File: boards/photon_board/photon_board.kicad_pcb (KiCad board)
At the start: 2 copper layers, 2 parts, among them J1 TERASIC, J2 PHOTON

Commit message: finalize schematic
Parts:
- added C1: 1u, Capacitor_SMD:C_0603_1608Metric_Pad1.05x0.95mm_HandSolder, F.Cu at (151.5, 79.5)
- added C2: 0.1u, Capacitor_SMD:C_0603_1608Metric_Pad1.05x0.95mm_HandSolder, F.Cu at (151.5, 81.0)
- added C3: 1u, Capacitor_SMD:C_0603_1608Metric_Pad1.05x0.95mm_HandSolder, F.Cu at (154.9, 79.5)
- added C4: 0.1u, Capacitor_SMD:C_0603_1608Metric_Pad1.05x0.95mm_HandSolder, F.Cu at (154.9, 81.0)
- added U1: SN65LVDT34D, Package_SO:SOIC-8_3.9x4.9mm_P1.27mm, F.Cu at (163.8, 71.3)
- added U2: SN65LVDT34D, Package_SO:SOIC-8_3.9x4.9mm_P1.27mm, F.Cu at (163.7, 80.6)
- J1: moved to B.Cu
- moved J2 13.5 mm to (175.8, 79.4)
- turned J1 to 180 degrees
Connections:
- J1 pad 18: Net-(J1-Pad18) -> /DATA_CLK
- J1 pad 20: Net-(J1-Pad20) -> /DATA2_OUT
- J1 pad 22: Net-(J1-Pad22) -> /DATA1_OUT
- J1 pad 24: Net-(J1-Pad24) -> /DATA_SYNC
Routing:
- net /DATA2_OUT-: track 5.44 -> 0.00 mm
- net /DATA_CLK+: track 5.30 -> 0.00 mm
- net /DATA_CLK-: track 5.15 -> 0.00 mm
- net /DATA2_OUT+: track 3.95 -> 0.00 mm

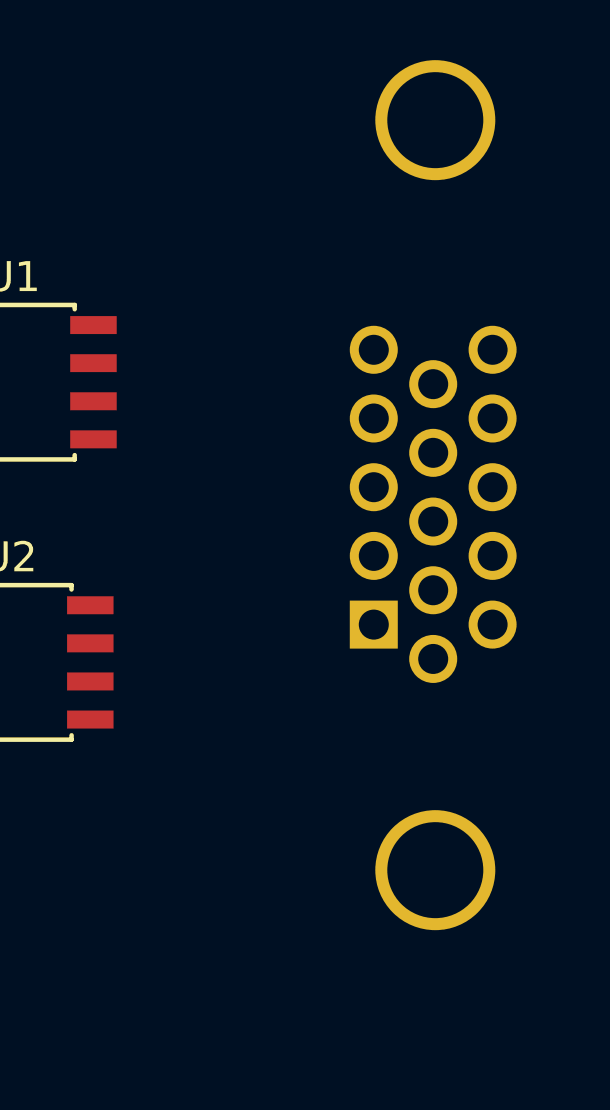
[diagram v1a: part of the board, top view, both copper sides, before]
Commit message: add connector for photon and make appropriate footprint
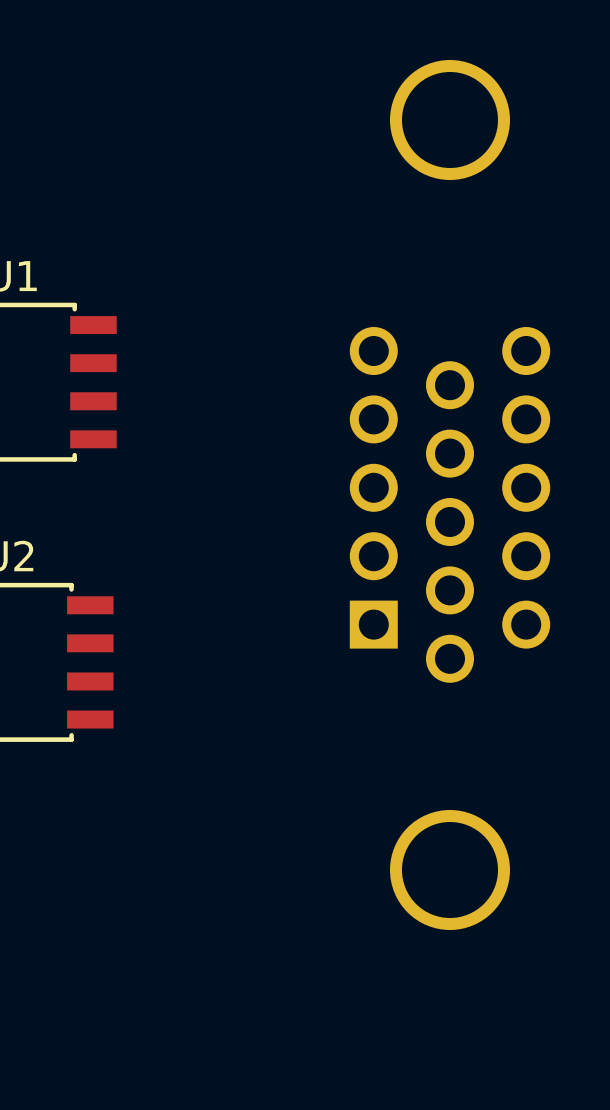
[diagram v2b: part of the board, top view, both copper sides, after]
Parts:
- J2: footprint Connector_Dsub:DSUB-15-HD_Female_Horizontal_P2.29x1.98mm_EdgePinOffset3.03mm_Housed_MountingHolesOffset4.94mm -> d_connector:DSUB-15-HD_Female_Horizontal_Pitch2.28x2.54mm_EdgePinOffset8.89mm_Housed_MountingHolesOffset11.43mm

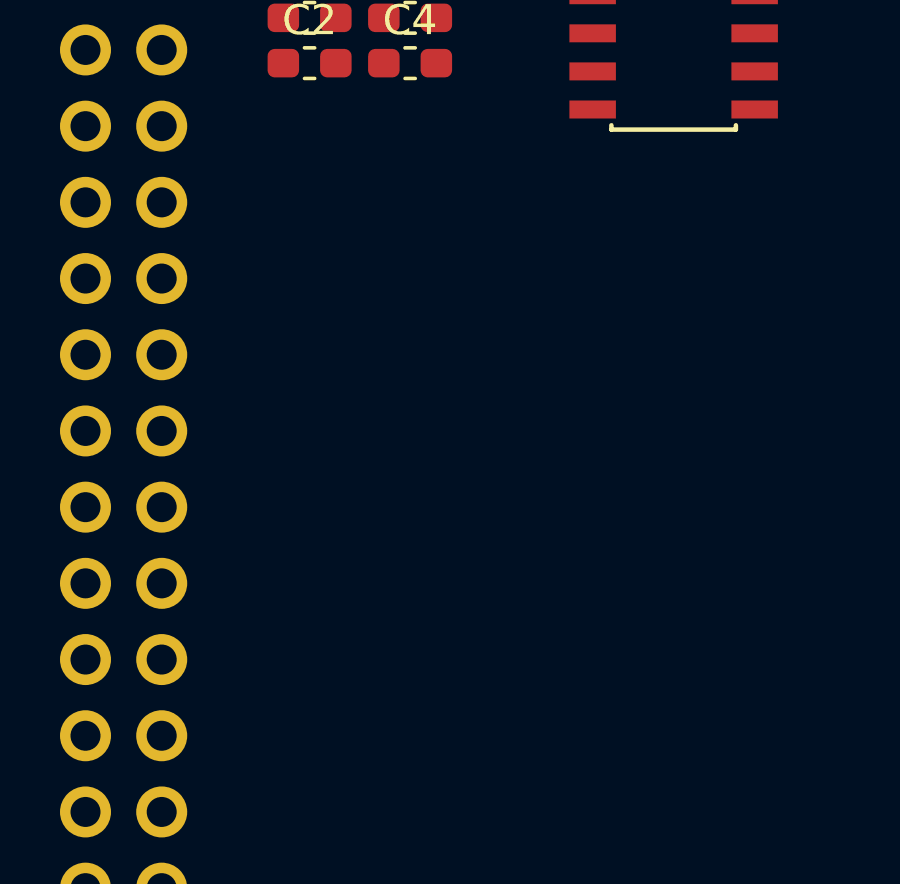
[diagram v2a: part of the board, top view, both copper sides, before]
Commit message: add data out connector for eg logic analysis
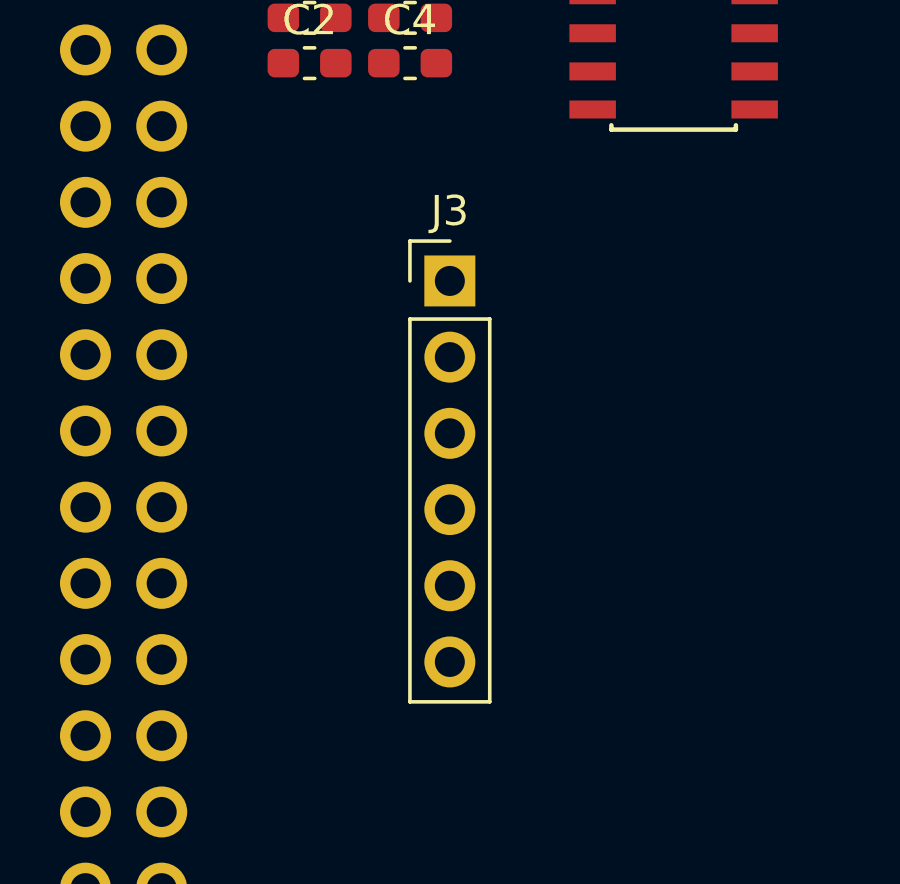
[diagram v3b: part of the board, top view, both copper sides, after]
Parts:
- added J3: DATA, Connector_PinHeader_2.54mm:PinHeader_1x06_P2.54mm_Vertical, F.Cu at (156.2, 88.3)
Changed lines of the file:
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@@
     (tracks 0)
     (zones 0)
-    (modules 8)
+    (modules 9)
     (nets 54)
   )
@@
     )
   )
+  (module Connector_PinHeader_2.54mm:PinHeader_1x06_P2.54mm_Vertical (layer F.Cu)
+    (at 156.21 88.265)
+    (descr "Through hole straight pin header, 1x06, 2.54mm pitch, single row")
+    (tags "Through hole pin header THT 1x06 2.54mm single row")
+    (fp_text reference J3 (at 0 -2.33) (layer F.SilkS)
+      (effects (font (size 1 1) (thickness 0.15)))
+    )
+    (fp_text value DATA (at 0 15.03) (layer F.Fab)
+      (effects (font (size 1 1) (thickness 0.15)))
+    )
+    (fp_line (start -0.635 -1.27) (end 1.27 -1.27) (layer F.Fab) (width 0.1))
+    (fp_line (start 1.27 -1.27) (end 1.27 13.97) (layer F.Fab) (width 0.1))
+    (fp_line (start 1.27 13.97) (end -1.27 13.97) (layer F.Fab) (width 0.1))
+    (fp_line (start -1.27 13.97) (end -1.27 -0.635) (layer F.Fab) (width 0.1))
+    (fp_line (start -1.27 -0.635) (end -0.635 -1.27) (layer F.Fab) (width 0.1))
+    (fp_line (start -1.33 14.03) (end 1.33 14.03) (layer F.SilkS) (width 0.12))
+    (fp_line (start -1.33 1.27) (end -1.33 14.03) (layer F.SilkS) (width 0.12))
+    (fp_line (start 1.33 1.27) (end 1.33 14.03) (layer F.SilkS) (width 0.12))
+    (fp_line (start -1.33 1.27) (end 1.33 1.27) (layer F.SilkS) (width 0.12))
+    (fp_line (start -1.33 0) (end -1.33 -1.33) (layer F.SilkS) (width 0.12))
+    (fp_line (start -1.33 -1.33) (end 0 -1.33) (layer F.SilkS) (width 0.12))
+    (fp_line (start -1.8 -1.8) (end -1.8 14.5) (layer F.CrtYd) (width 0.05))
+    (fp_line (start -1.8 14.5) (end 1.8 14.5) (layer F.CrtYd) (width 0.05))
+    (fp_line (start 1.8 14.5) (end 1.8 -1.8) (layer F.CrtYd) (width 0.05))
+    (fp_line (start 1.8 -1.8) (end -1.8 -1.8) (layer F.CrtYd) (width 0.05))
+    (fp_text user %R (at 0 6.35 90) (layer F.Fab)
+      (effects (font (size 1 1) (thickness 0.15)))
+    )
+    (pad 1 thru_hole rect (at 0 0) (size 1.7 1.7) (drill 1) (layers *.Cu *.Mask)
+      (net 12 GND))
+    (pad 2 thru_hole oval (at 0 2.54) (size 1.7 1.7) (drill 1) (layers *.Cu *.Mask)
+      (net 50 /DATA_CLK))
+    (pad 3 thru_hole oval (at 0 5.08) (size 1.7 1.7) (drill 1) (layers *.Cu *.Mask)
+      (net 51 /DATA2_OUT))
+    (pad 4 thru_hole oval (at 0 7.62) (size 1.7 1.7) (drill 1) (layers *.Cu *.Mask)
+      (net 52 /DATA1_OUT))
+    (pad 5 thru_hole oval (at 0 10.16) (size 1.7 1.7) (drill 1) (layers *.Cu *.Mask)
+      (net 53 /DATA_SYNC))
+    (pad 6 thru_hole oval (at 0 12.7) (size 1.7 1.7) (drill 1) (layers *.Cu *.Mask)
+      (net 12 GND))
+    (model ${KISYS3DMOD}/Connector_PinHeader_2.54mm.3dshapes/PinHeader_1x06_P2.54mm_Vertical.wrl
+      (at (xyz 0 0 0))
+      (scale (xyz 1 1 1))
+      (rotate (xyz 0 0 0))
+    )
+  )

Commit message: route board
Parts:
- moved U2 15.3 mm to (161.0, 95.8)
- moved J2 15.1 mm to (171.5, 93.8)
- moved U1 14.6 mm to (161.0, 85.6)
- moved C4 11.8 mm to (159.3, 91.9), turned to 180 degrees
- moved C3 11.5 mm to (159.3, 90.2)
- moved C2 7.76 mm to (159.3, 81.8), turned to 180 degrees
- moved C1 7.74 mm to (159.3, 80.0)
- moved J3 6.74 mm to (151.6, 83.3)
- moved J1 0.37 mm to (143.8, 65.5)
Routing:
- net +3V3: track 0.00 -> 78.4 mm, vias 0 -> 2
- net /DATA2_OUT-: track 0.00 -> 17.4 mm
- net /DATA_SYNC: track 0.00 -> 13.8 mm
- net /DATA1_OUT: track 0.00 -> 13.8 mm
- net /DATA_CLK: track 0.00 -> 13.8 mm
- net /DATA2_OUT: track 0.00 -> 13.8 mm
- net /DATA2_OUT+: track 0.00 -> 13.6 mm
- net /DATA_CLK+: track 0.00 -> 11.9 mm
- net /DATA_CLK-: track 0.00 -> 11.9 mm
- net /DATA_SYNC+: track 0.00 -> 11.4 mm
- net /DATA_SYNC-: track 0.00 -> 11.4 mm
- net /DATA1_OUT+: track 0.00 -> 11.3 mm
- net /DATA1_OUT-: track 0.00 -> 11.3 mm
- added copper zone on B.Cu, net GND
- added copper zone on F.Cu, net GND
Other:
- board outline added: 45 x 60 mm
- net class Default: via_dia 0.8 -> 0.508; via_drill 0.4 -> 0.254
- rule via_min_drill: 0.3 -> 0.254
- rule via_min_size: 0 -> 0.508

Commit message: do up silkscreen
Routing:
- net GND: vias 0 -> 14
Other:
- board text added: "1: GND 2: DATA_CLK 3: DATA2_OUT 4: DATA1_OUT 5: DATA_SYNC 6: GND"
- board text added: "Camerica - Photon Board by Thomas Watson"
- board text added: "Revision 1 2018-11-20"
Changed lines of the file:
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@@
   (general
     (thickness 1.6)
-    (drawings 4)
-    (tracks 414)
+    (drawings 12)
+    (tracks 427)
     (zones 0)
     (modules 9)
@@
     )
   )
+  (gr_text "Revision 1\n2018-11-20" (at 180.34 66.04 90) (layer F.SilkS)
+    (effects (font (size 1.5 1.5) (thickness 0.3)) (justify right))
+  )
+  (gr_text "Camerica - Photon Board\nby Thomas Watson" (at 180.34 114.3 90) (layer F.SilkS)
+    (effects (font (size 1.5 1.5) (thickness 0.3)) (justify left))
+  )
+  (gr_line (start 151.638 80.01) (end 152.146 79.502) (layer F.SilkS) (width 0.2))
+  (gr_line (start 151.13 79.502) (end 151.638 80.01) (layer F.SilkS) (width 0.2))
+  (gr_line (start 151.638 80.01) (end 151.13 79.502) (layer F.SilkS) (width 0.2))
+  (gr_line (start 151.638 79.248) (end 151.638 80.01) (layer F.SilkS) (width 0.2))
+  (gr_line (start 151.638 78.486) (end 151.638 79.248) (layer F.SilkS) (width 0.2))
+  (gr_text "1: GND\n2: DATA_CLK\n3: DATA2_OUT\n4: DATA1_OUT\n5: DATA_SYNC\n6: GND" (at 150.622 70.358) (layer F.SilkS)
+    (effects (font (size 1.5 1.5) (thickness 0.3)) (justify left))
+  )
   (gr_line (start 140 120) (end 140 60) (layer Edge.Cuts) (width 0.15))
   (gr_line (start 185 120) (end 140 120) (layer Edge.Cuts) (width 0.15))
   (gr_line (start 185 60) (end 185 120) (layer Edge.Cuts) (width 0.15))
   (gr_line (start 140 60) (end 185 60) (layer Edge.Cuts) (width 0.15))
+  (via (at 161.036 85.598) (size 1.016) (drill 0.508) (layers F.Cu B.Cu) (net 12))
+  (via (at 161.036 95.758) (size 1.016) (drill 0.508) (layers F.Cu B.Cu) (net 12))
+  (via (at 167.132 89.916) (size 1.016) (drill 0.508) (layers F.Cu B.Cu) (net 12))
+  (via (at 154.432 88.392) (size 1.016) (drill 0.508) (layers F.Cu B.Cu) (net 12))
+  (via (at 152.4 113.284) (size 1.016) (drill 0.508) (layers F.Cu B.Cu) (net 12))
+  (via (at 155.702 116.84) (size 1.016) (drill 0.508) (layers F.Cu B.Cu) (net 12))
+  (via (at 158.242 106.172) (size 1.016) (drill 0.508) (layers F.Cu B.Cu) (net 12))
+  (via (at 153.162 105.41) (size 1.016) (drill 0.508) (layers F.Cu B.Cu) (net 12))
+  (via (at 141.478 118.364) (size 1.016) (drill 0.508) (layers F.Cu B.Cu) (net 12))
+  (via (at 159.258 76.2) (size 1.016) (drill 0.508) (layers F.Cu B.Cu) (net 12))
+  (via (at 177.8 64.516) (size 1.016) (drill 0.508) (layers F.Cu B.Cu) (net 12))
+  (via (at 165.1 62.738) (size 1.016) (drill 0.508) (layers F.Cu B.Cu) (net 12))
+  (via (at 182.626 117.856) (size 1.016) (drill 0.508) (layers F.Cu B.Cu) (net 12))
+  (via (at 142.748 62.23) (size 1.016) (drill 0.508) (layers F.Cu B.Cu) (net 12))
   (segment (start 143.764 101.092) (end 140.97 103.886) (width 0.635) (layer B.Cu) (net 25) (status 10))
   (segment (start 140.97 103.886) (end 140.97 115.316) (width 0.635) (layer B.Cu) (net 25))
@@
   (segment (start 167.697214 86.905661) (end 167.757741 86.876515) (width 0.2032) (layer F.Cu) (net 38))
   (segment (start 168.077842 86.609066) (end 168.143337 86.594117) (width 0.2032) (layer F.Cu) (net 38))
-  (segment (start 171.438165 89.281835) (end 171.46 89.26) (width 0.125) (layer F.Cu) (net 38) (status 30))
   (segment (start 171.46 89.26) (end 170.7264 89.9936) (width 0.2032) (layer F.Cu) (net 38) (status 10))
   (segment (start 170.7264 89.9936) (end 170.54497 89.9936) (width 0.2032) (layer F.Cu) (net 38))
